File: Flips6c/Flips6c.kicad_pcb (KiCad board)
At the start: 2 copper layers, 90 x 50 mm, 23 parts, among them CN1 Conn_02x04_Odd_Even, U1 74HCT595, U2 74HCT595, U3 74HC238, U4 74HC238, U5 74LVC1G04

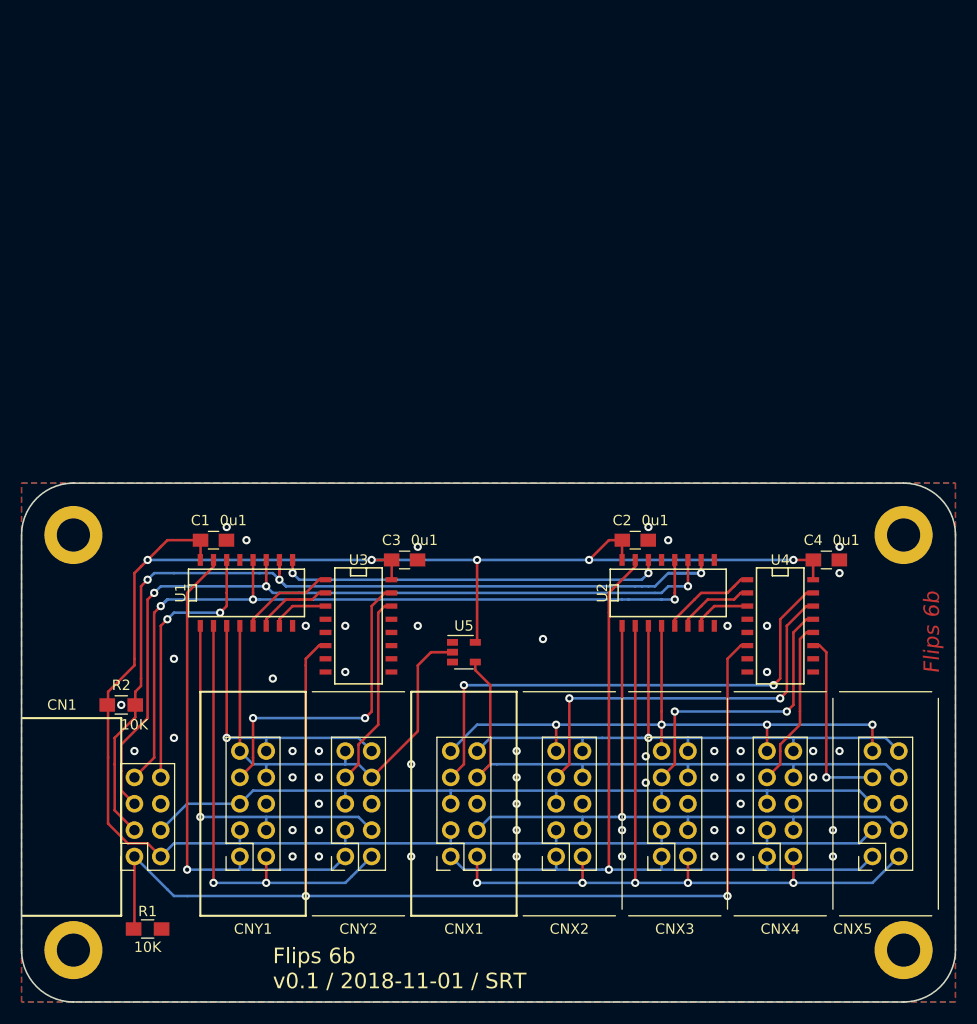
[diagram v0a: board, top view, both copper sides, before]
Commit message: partial pcb layout / routing of Flips6c
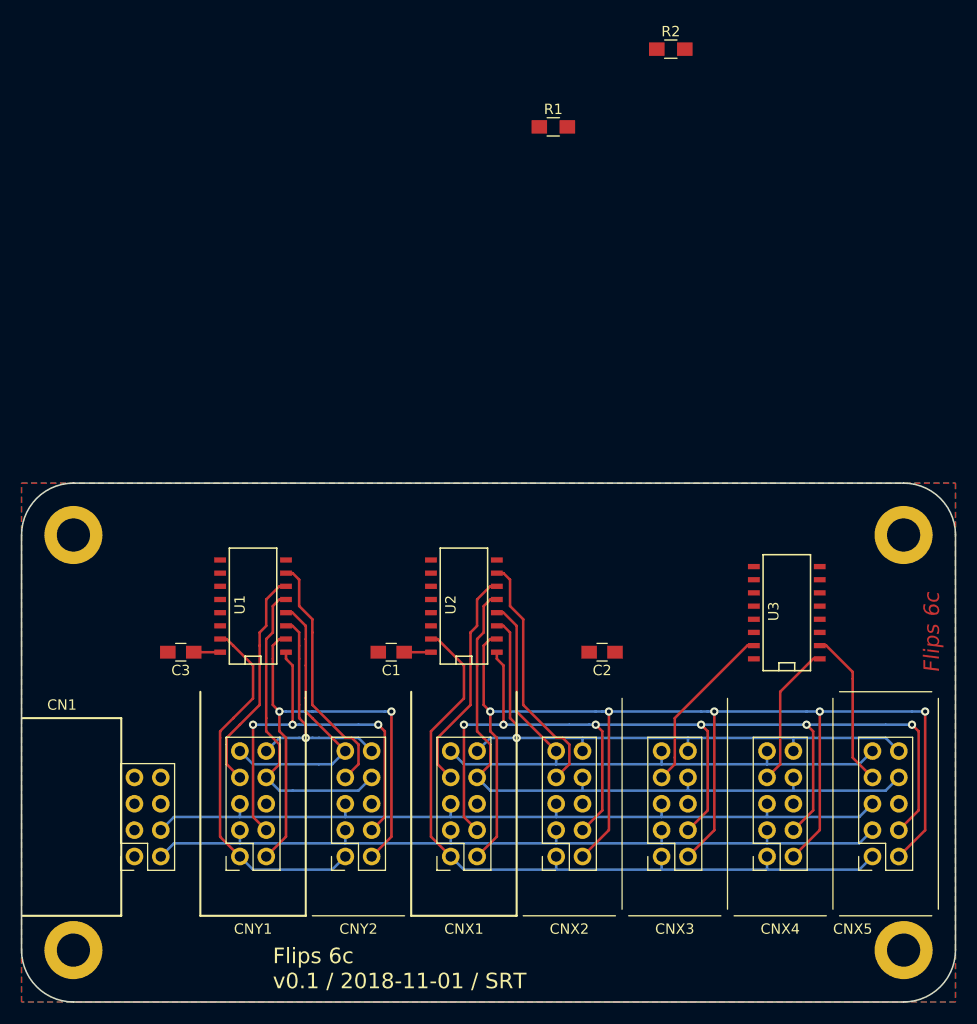
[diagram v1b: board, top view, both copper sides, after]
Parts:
- removed C4: 0u1, Capacitors_SMD:C_0805_HandSoldering
- removed U4: 74HC238, SMD_Packages:SO-16-N
- removed U5: 74LVC1G04, TO_SOT_Packages_SMD:SOT-23-5
- U3: value 74HC238 -> 74HCT595
- moved R1 86.6 mm to (223.2, 23.7)
- moved R2 82.4 mm to (234.6, 16.2), turned to 0 degrees
- moved U3 41.3 mm to (245.7, 70.5), turned to 90 degrees
- moved C3 23.3 mm to (187.3, 74.3), turned to 180 degrees
- moved C1 20.2 mm to (207.6, 74.3), turned to 180 degrees
- moved U2 19.7 mm to (214.6, 69.8), turned to 90 degrees
- moved C2 11.3 mm to (227.9, 74.3), turned to 180 degrees
- moved U1 1.42 mm to (194.3, 69.8), turned to 90 degrees
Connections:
- net /XA0 renamed /XA.0
- net /XA1 renamed /XA.1
- net /XA2 renamed /XA.2
- net /XB0 renamed /XB.0
- net /XB1 renamed /XB.1
- net /YA0 renamed /YA.0
- net /YA1 renamed /YA.1
- net /YA2 renamed /YA.2
- net /YB0 renamed /YB.0
- CN1 pad 1: /ENABLE -> /~OE
- CNX1 pad 7: /XE.0 -> /XEN1
- CNX1 pad 8: /XD -> /XDAT
- CNX2 pad 7: /XE.1 -> /XEN2
- CNX2 pad 8: /XD -> /XDAT
- CNX3 pad 7: /XE.2 -> /XEN3
- CNX3 pad 8: /XD -> /XDAT
- CNX4 pad 7: /XE.3 -> /XEN4
- CNX4 pad 8: /XD -> /XDAT
- CNX5 pad 7: /XE.4 -> /XEN5
- CNX5 pad 8: /XD -> /XDAT
- CNY1 pad 7: /YE.0 -> /YEN1
- CNY1 pad 8: /POL -> /YDAT
- CNY1 pad 9: /POL -> /YB.1
- CNY2 pad 7: /YE.1 -> /YEN2
- CNY2 pad 8: /POL -> /YDAT
- CNY2 pad 9: /POL -> /YB.1
- R1 pad 1: /ENABLE -> /~OE
- R1 pad 2: GND -> +5V
- U1 pad 13: GND -> /~OE
- U1 pad 4: /POL -> /YB.1
- U1 pad 5: /YC0 -> /YDAT
- U1 pad 6: /YC1 -> /YEN1
- U1 pad 7: /YC2 -> /YEN2
- U2 pad 13: GND -> /~OE
- U2 pad 5: /XC0 -> /XDAT
- U2 pad 6: /XC1 -> /XEN1
- U2 pad 7: /XC2 -> /XEN2
- U2 pad 9: (no net) -> /DIN
- U3 pad 1: /YC0 -> /XEN4
- U3 pad 10: (no net) -> /~SRCLR
- U3 pad 11: (no net) -> /SRCLK
- U3 pad 12: /YE.3 -> /RCLK
- U3 pad 13: /YE.2 -> /~OE
- U3 pad 14: /YE.1 -> /DIN
- U3 pad 15: /YE.0 -> /XEN3
- U3 pad 2: /YC1 -> /XEN5
- U3 pad 3: /YC2 -> (no net)
- U3 pad 4: GND -> (no net)
- U3 pad 5: GND -> (no net)
- U3 pad 6: /ENABLE -> (no net)
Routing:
- net +5V: track 202.2 -> 82.4 mm, vias 5 -> 0
- net /ENABLE: track 116.3 -> 0.00 mm, vias 2 -> 0
- net /~SRCLR: track 90.0 -> 0.00 mm, vias 3 -> 0
- net /SRCLK: track 79.5 -> 0.00 mm, vias 3 -> 0
- net /RCLK: track 76.5 -> 0.00 mm, vias 3 -> 0
- net /XDAT: track 0.00 -> 64.9 mm
- net /XD: track 57.7 -> 0.00 mm
- net /XE.0: track 50.1 -> 0.00 mm, vias 2 -> 0
- net /XA.2: track 76.6 -> 125.2 mm
- net /POL: track 44.9 -> 0.00 mm
- net /XA.1: track 63.9 -> 106.0 mm, vias 1 -> 6
- net /XE.1: track 39.0 -> 0.00 mm, vias 2 -> 0
- net Net-(U1-Pad9): track 37.4 -> 0.00 mm, vias 2 -> 0
- net /YDAT: track 0.00 -> 30.6 mm
- net /YE.0: track 30.5 -> 0.00 mm, vias 2 -> 0
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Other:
- board text added: "Flips 6c"
- board text added: "Flips 6c v0.1 / 2018-11-01 / SRT"
- board text removed: "Flips 6b"
- board text removed: "Flips 6b v0.1 / 2018-11-01 / SRT"

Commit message: finish tracing PCB for flips6c
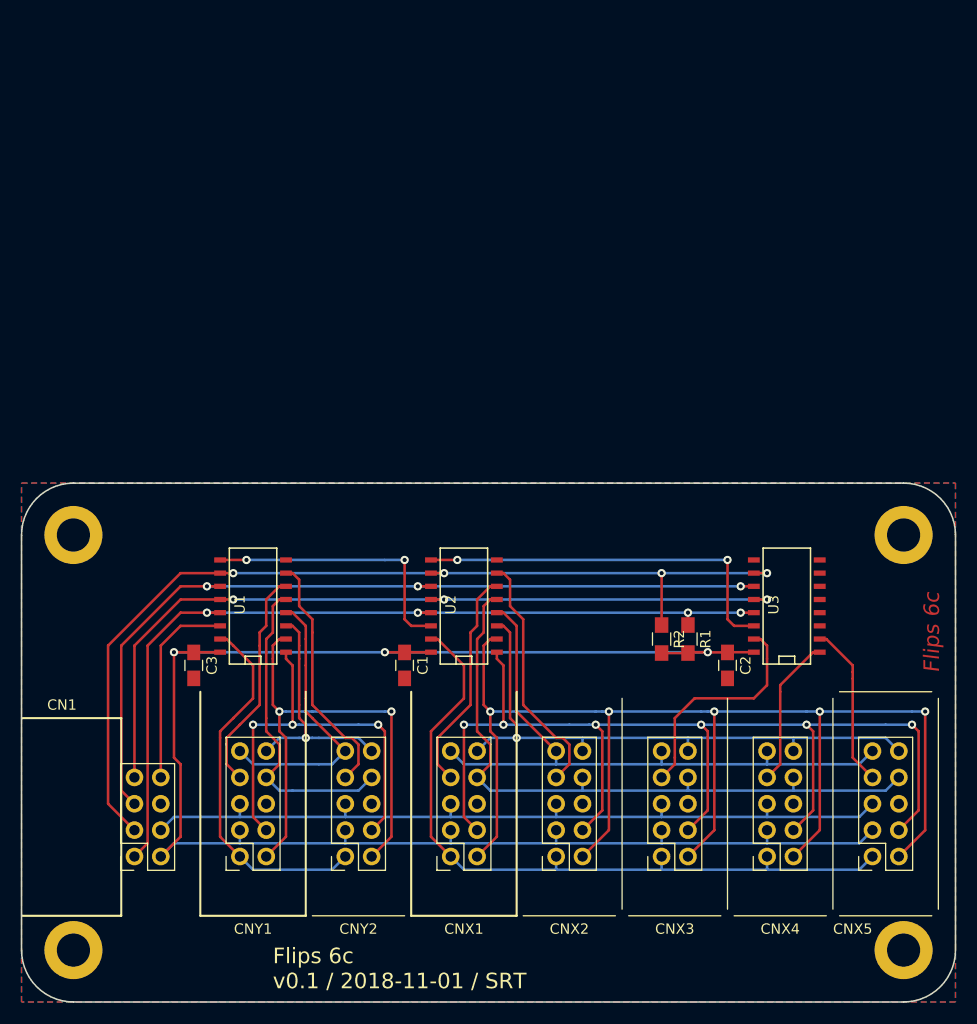
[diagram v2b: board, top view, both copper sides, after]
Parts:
- moved R2 56.9 mm to (233.7, 73.0), turned to 270 degrees
- moved R1 51.0 mm to (236.2, 73.0), turned to 270 degrees
- moved C2 12.2 mm to (240.0, 75.6), turned to 270 degrees
- moved C1 1.81 mm to (208.9, 75.6), turned to 270 degrees
- moved C3 1.78 mm to (188.6, 75.6), turned to 270 degrees
- moved U3 0.64 mm to (245.7, 69.8)
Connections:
- U2 pad 9: /DIN -> Net-(U2-Pad9)
- U3 pad 14: /DIN -> Net-(U2-Pad9)
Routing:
- net /~SRCLR: track 0.00 -> 92.8 mm, vias 0 -> 4
- net +5V: track 82.4 -> 167.3 mm, vias 0 -> 3
- net /~OE: track 0.00 -> 84.3 mm, vias 0 -> 4
- net /SRCLK: track 0.00 -> 81.6 mm, vias 0 -> 3
- net /RCLK: track 0.00 -> 78.0 mm, vias 0 -> 3
- net Net-(U2-Pad9): track 0.00 -> 37.1 mm, vias 0 -> 2
- net Net-(U1-Pad9): track 0.00 -> 26.3 mm, vias 0 -> 2
- net /DIN: track 0.00 -> 19.2 mm
- net /XEN3: track 16.8 -> 21.8 mm
- net /XEN4: track 13.9 -> 14.5 mm
- net /XEN5: track 15.2 -> 15.8 mm

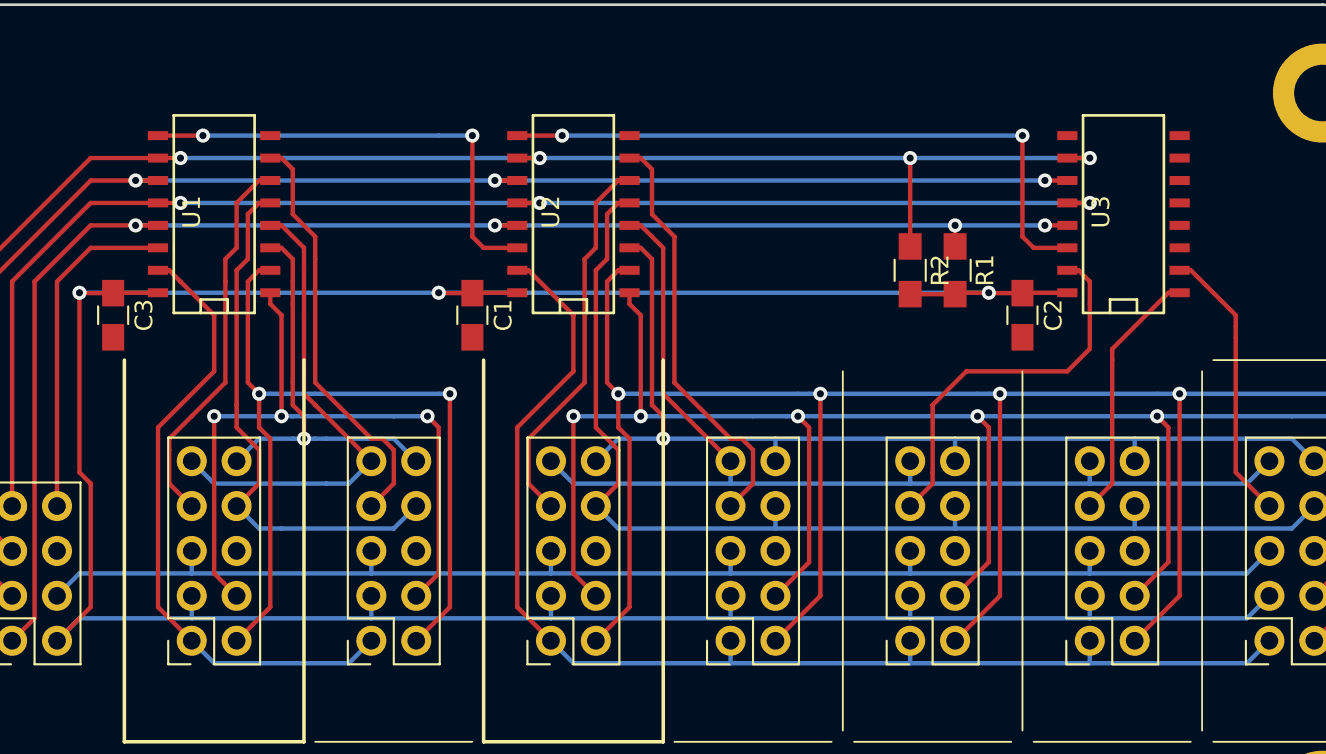
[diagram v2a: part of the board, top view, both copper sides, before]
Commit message: moving pullups into small gap, leaving space for text/labels
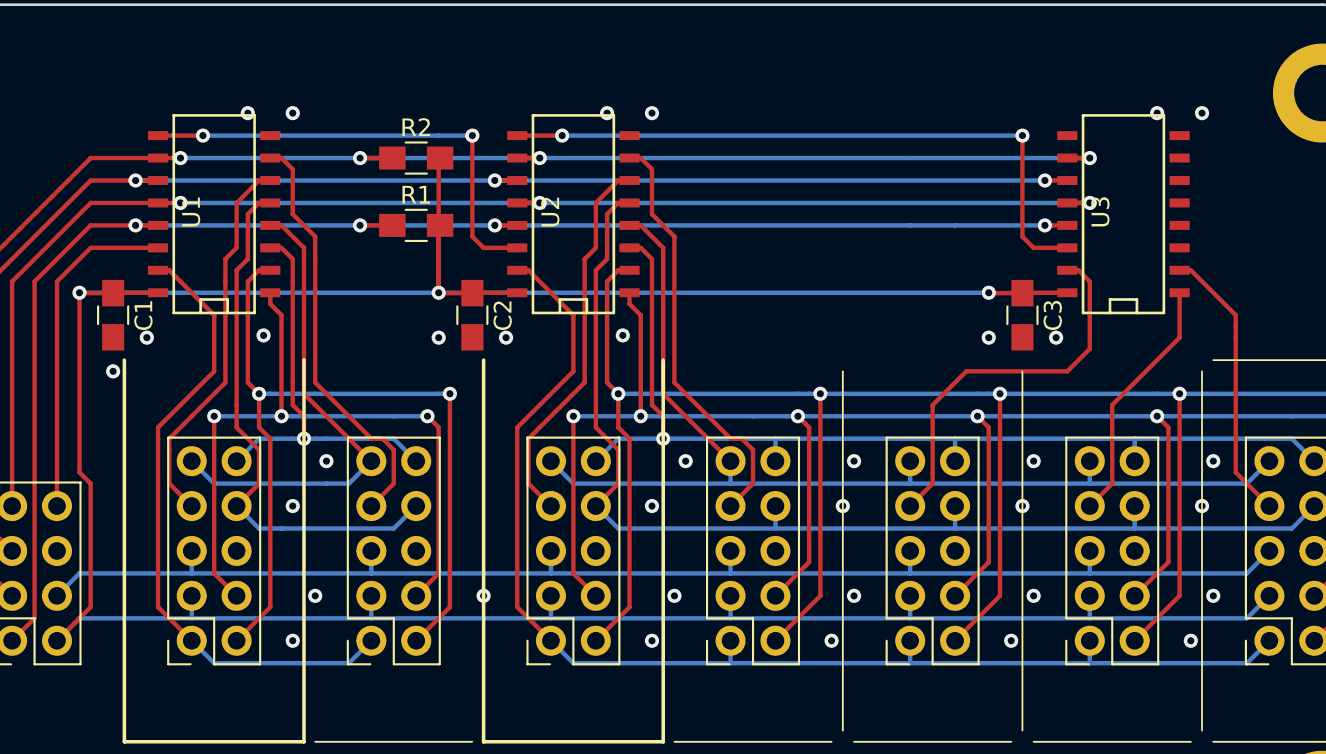
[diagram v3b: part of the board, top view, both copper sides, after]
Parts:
- moved C3 51.4 mm to (240.0, 75.6)
- moved C2 31.1 mm to (208.9, 75.6)
- moved R1 30.6 mm to (205.7, 70.5), turned to 0 degrees
- moved R2 28.7 mm to (205.7, 66.7), turned to 0 degrees
- moved C1 20.3 mm to (188.6, 75.6)
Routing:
- net +5V: track 167.3 -> 174.3 mm
- net /~SRCLR: track 92.8 -> 89.6 mm
- net /~OE: track 84.3 -> 84.9 mm
- net GND: vias 0 -> 35

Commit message: minor tweaks
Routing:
- net /YA.1: track 40.9 -> 41.8 mm
- net /YA.2: track 48.7 -> 49.6 mm
- net /~SRCLR: track 89.6 -> 89.1 mm
- net GND: vias 35 -> 48
